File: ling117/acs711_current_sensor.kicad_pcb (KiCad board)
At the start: 2 copper layers, 36.3 x 33.3 mm, 11 parts, among them J1 Conn_01x02_Socket, J2 Conn_01x02_Socket, U1 ACS711xLCTR-12AB, U2 mcp6546-e/p

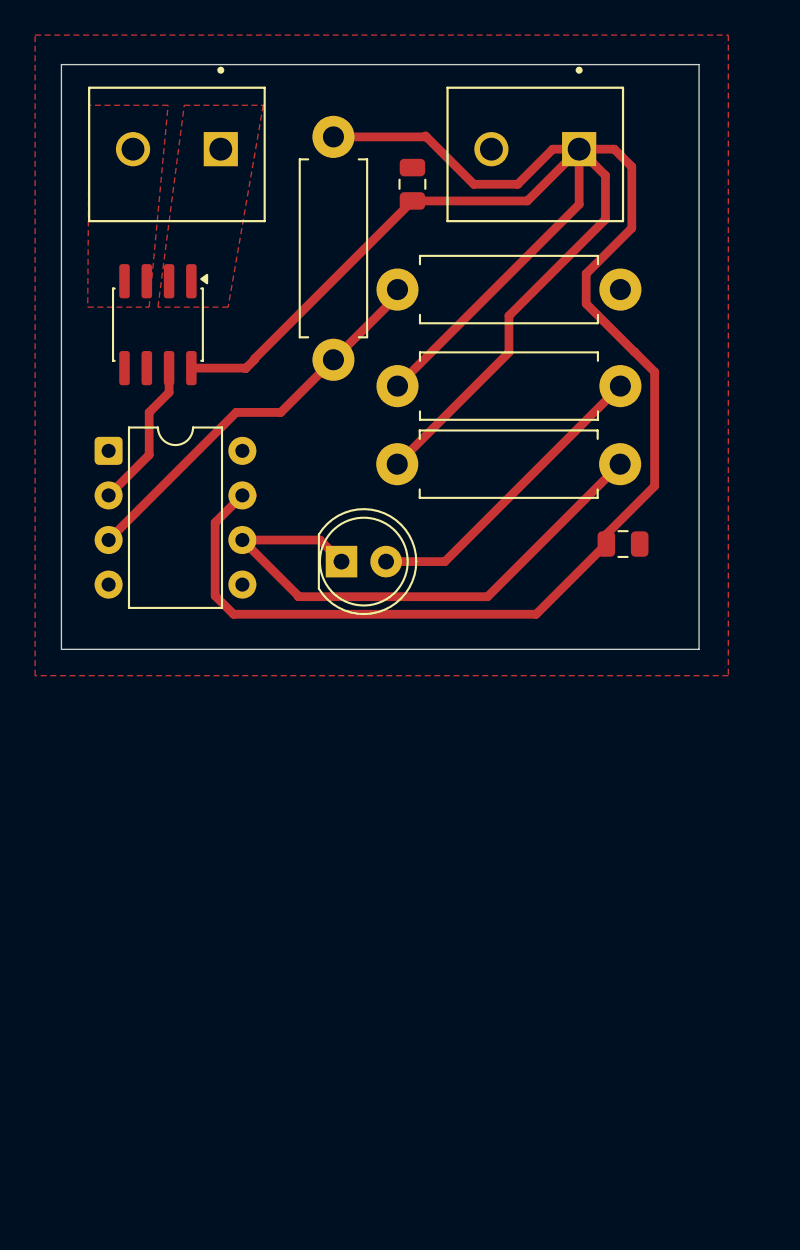
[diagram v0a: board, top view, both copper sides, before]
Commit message: fixed throughhole layer and decoupling capacitors
put all through hole components on back copper layer and moved decoupling capacitors closer to the actual component
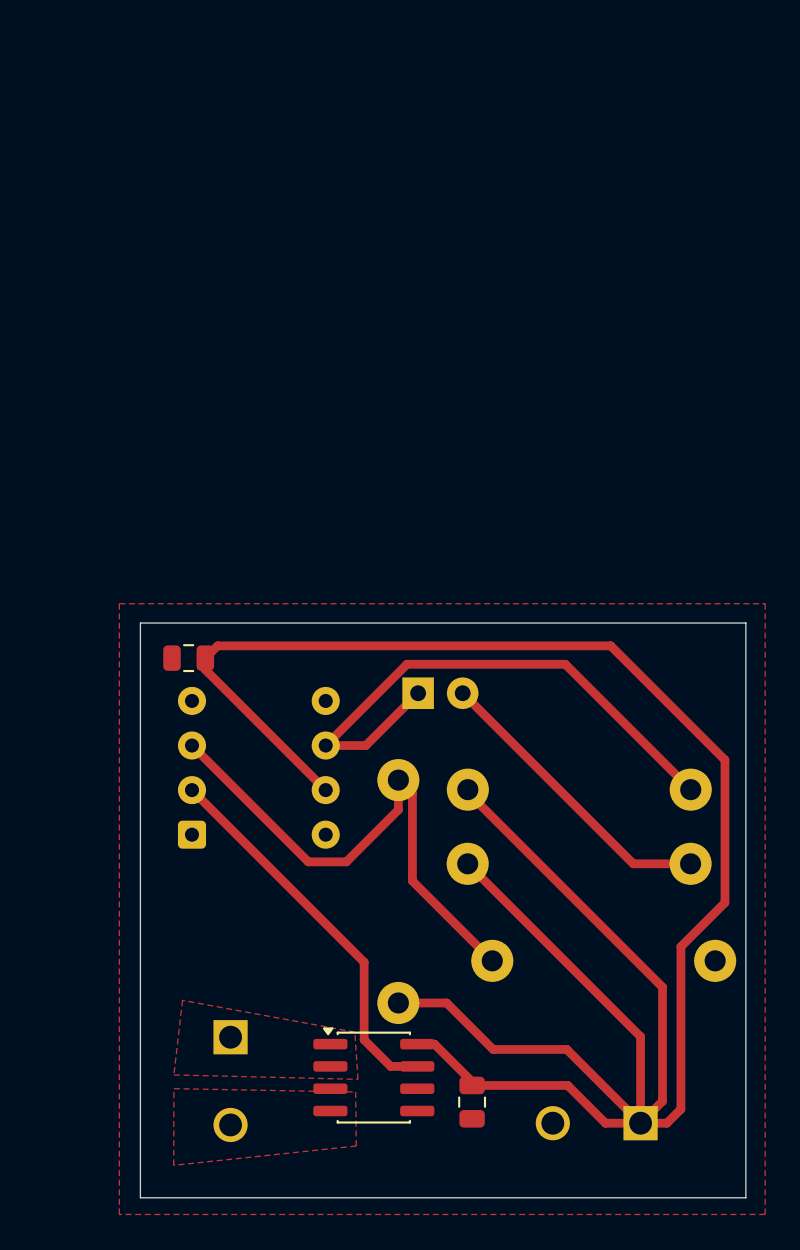
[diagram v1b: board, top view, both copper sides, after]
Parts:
- D2, J1, J2, R1, R2, R3, R5, U2: moved to B.Cu
- moved J1 55.6 mm to (132.5, 131.0)
- moved C2 52.4 mm to (122.9, 129.8), turned to 90 degrees
- moved J2 50.6 mm to (109.1, 126.1), turned to -90 degrees
- moved R2 49.5 mm to (118.7, 124.2), turned to 90 degrees
- moved U1 44.6 mm to (117.3, 128.4), turned to 0 degrees
- moved R3 38.6 mm to (124.0, 121.8)
- moved R5 27.5 mm to (135.3, 116.2)
- moved C1 25.6 mm to (106.8, 104.5), turned to 0 degrees
- moved U2 22.4 mm to (106.9, 114.6)
- moved R1 19.0 mm to (135.4, 112.0)
- moved D2 8.68 mm to (119.8, 106.5)
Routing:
- net Sensor Output: track 8.68 -> 21.9 mm
- net Reference Voltage: track 22.6 -> 30.0 mm
- net +3V3: track 145.4 -> 140.8 mm
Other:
- board size 36.3 x 33.3 mm -> 34.5 x 32.8 mm
